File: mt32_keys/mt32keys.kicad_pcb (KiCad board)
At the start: 2 copper layers, 104.1 x 27.9 mm, 31 parts, among them CN4 Conn_01x02, CN5 Conn_01x07, SW11 KLS7, SW12 KLS7, SW13 KLS7, SW14 KLS7, SW15 KLS7, SW16 KLS7, SW17 KLS7, SW18 KLS7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

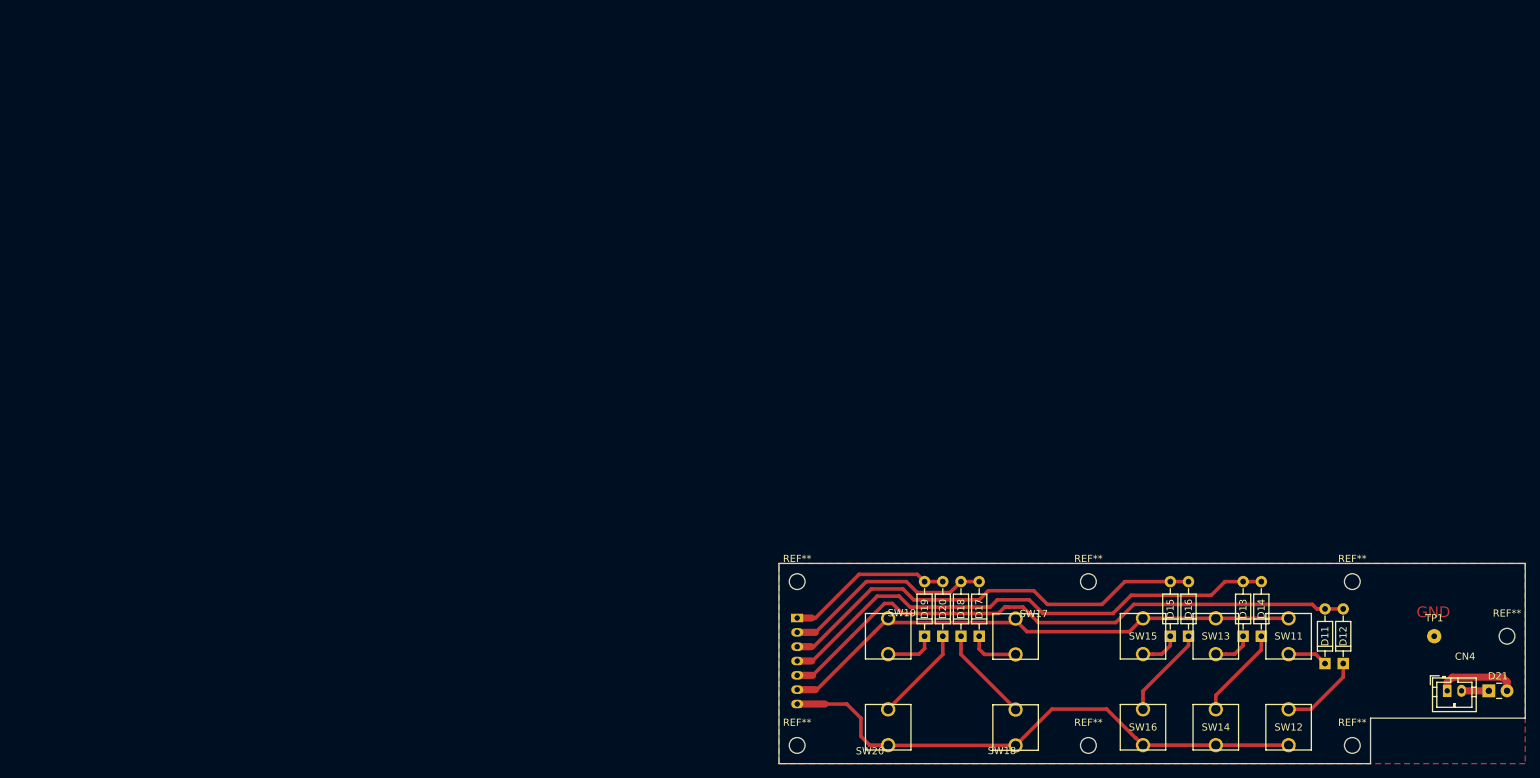
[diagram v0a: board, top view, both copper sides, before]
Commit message: Updated for real size
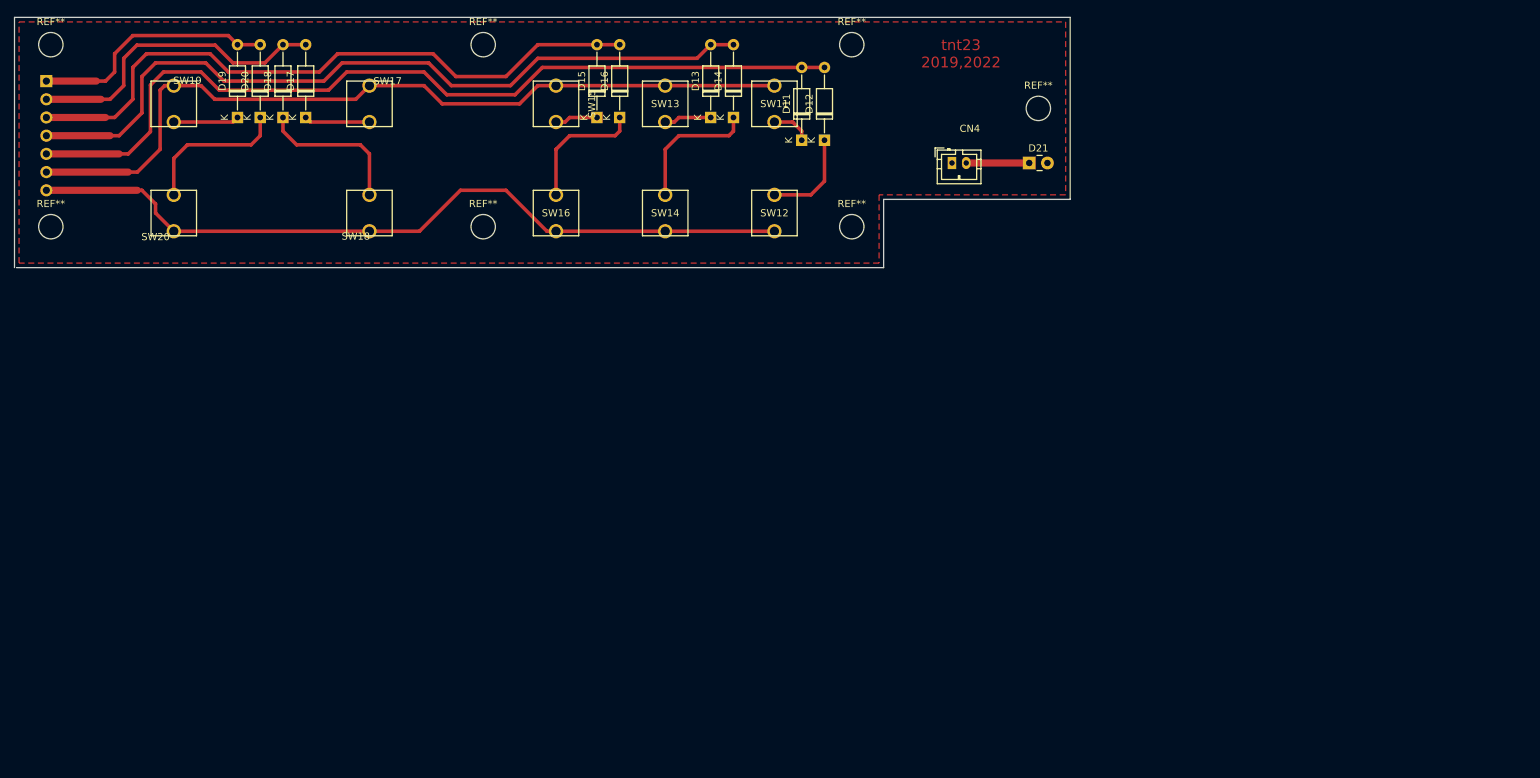
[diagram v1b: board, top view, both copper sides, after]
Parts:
- removed TP1: GND, Wire_Pads:SolderWirePad_single_0-8mmDrill
- CN5: footprint Connectors_JST:JST_PH_B7B-PH-K_07x2.00mm_Straight -> Connector_PinHeader_2.54mm:PinHeader_1x07_P2.54mm_Vertical
- D11, D12, D13, D14, D15, D16, D17, D18, D19, D20: footprint Diodes_THT:D_DO-35_SOD27_P7.62mm_Horizontal -> Diode_THT:D_DO-35_SOD27_P10.16mm_Horizontal
- moved CN5 128.8 mm to (4.45, 8.89), turned to 180 degrees
- moved REF** 128.3 mm to (5.07, 3.81)
- moved REF** 126.8 mm to (5.07, 29.2)
- moved SW19 124.3 mm to (22.2, 12.1)
- moved SW20 122.8 mm to (22.2, 27.3)
- moved D19 120.1 mm to (31.1, 14.0)
- moved D20 119.6 mm to (34.3, 14.0)
- moved D18 119.1 mm to (37.5, 14.0)
- moved D17 118.6 mm to (40.6, 14.0)
- moved SW17 116.9 mm to (49.5, 12.1)
- moved SW18 115.3 mm to (49.5, 27.3)
- moved REF** 112.9 mm to (65.4, 3.81)
- moved REF** 111.2 mm to (65.4, 29.2)
- moved SW15 110.6 mm to (75.6, 12.1)
- moved SW16 108.9 mm to (75.6, 27.3)
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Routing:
- net /SC_1: track 74.9 -> 115.1 mm
- net /SC_0: track 76.7 -> 109.4 mm
- net /SI_2: track 61.3 -> 91.6 mm
- net /SI_1: track 81.1 -> 108.9 mm
- net /SI_3: track 29.6 -> 43.6 mm
- net /VCC: track 11.4 -> 0.00 mm
- net /SI_4: track 23.3 -> 34.5 mm
- net /SI_0: track 113.5 -> 122.1 mm
- net Net-(D20-Pad1): track 13.4 -> 21.0 mm
- net Net-(D18-Pad1): track 13.4 -> 21.0 mm
- net Net-(D14-Pad1): track 12.8 -> 18.8 mm
- net Net-(D16-Pad1): track 12.8 -> 18.2 mm
- net /LED: track 3.81 -> 8.79 mm
- net Net-(D12-Pad1): track 11.4 -> 13.5 mm
- net Net-(D19-Pad1): track 7.12 -> 9.15 mm
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- added copper zone on F.Cu, net /VCC
- removed copper zone on F.Cu, net GND
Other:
- board size 104.1 x 27.9 mm -> 147.3 x 34.9 mm
- net class Default removed
- board text added: "Original SW board is 148 mm x 35 mm"
- board text added: "tnt23 2019,2022"
- board text removed: "GND"
- board text removed: "Original SW board is 148 mm x 25.5 mm"
- board text removed: "Original: 25.5mm"
- board text removed: "Original: 27mm"

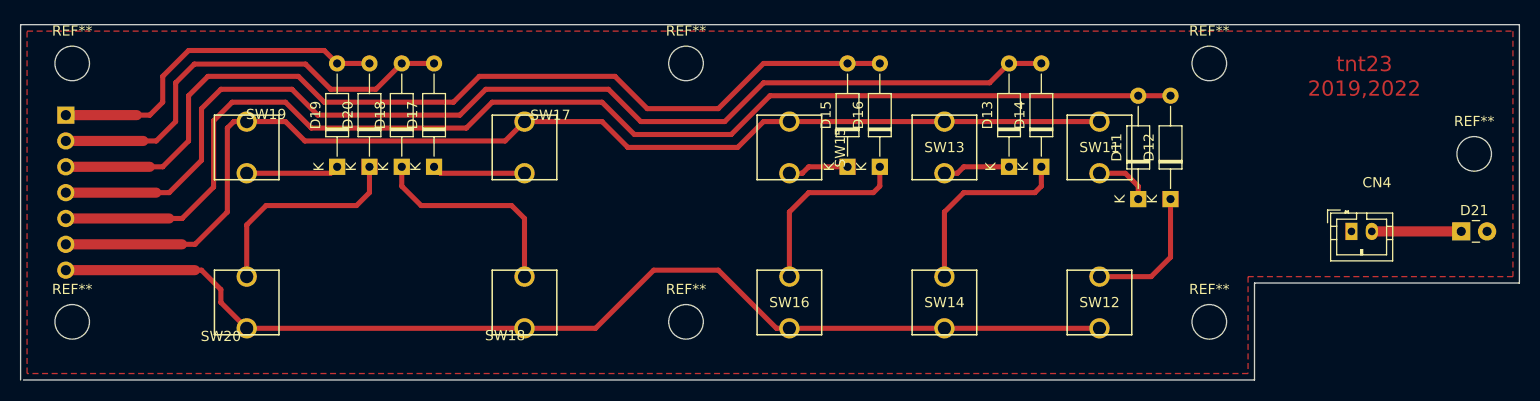
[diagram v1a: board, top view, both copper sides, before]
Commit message: Update 3d models and silk
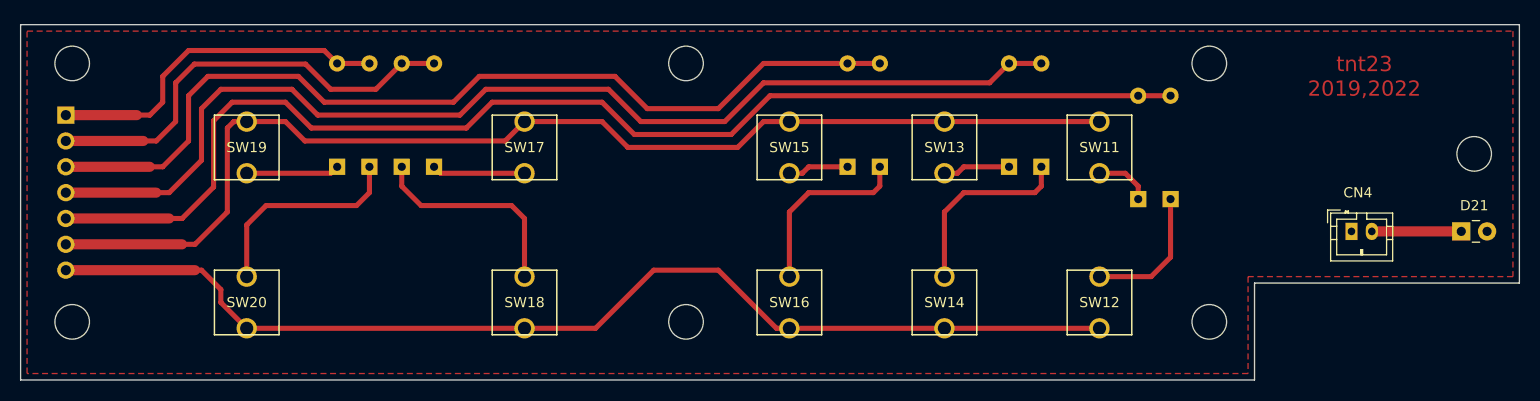
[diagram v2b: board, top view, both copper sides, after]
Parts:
- D11, D12, D13, D14, D15, D16, D17, D18, D19, D20: moved to B.Cu
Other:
- outline, holes or cut-outs redrawn

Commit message: Update PCB
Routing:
- net /SC_1: track 115.1 -> 113.8 mm
- net /SC_0: track 109.4 -> 108.7 mm
- net /SI_2: track 91.6 -> 91.0 mm
- net /SI_3: track 43.6 -> 43.1 mm
- net /SI_1: track 108.9 -> 108.3 mm
